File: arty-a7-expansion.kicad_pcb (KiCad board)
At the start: 4 copper layers, 109.2 x 47 mm, 119 parts, among them IC1 TPD8S009DSMR, IC2 PCA9500PW, J1 SJ-43516-SMT-GR, J2 1140084168, J3 SJ-43516-SMT-BE, J4 685119134923, J5 UE27AC54100, U1 TPS61232DRCT, U2 MAX3421EEHJ, U3 CS4344-CZZ, U4 CS5343-CZZ, U5 NC7SZ126P5X, Y1 ABM8G-12.000MHZ-18-D2Y-T

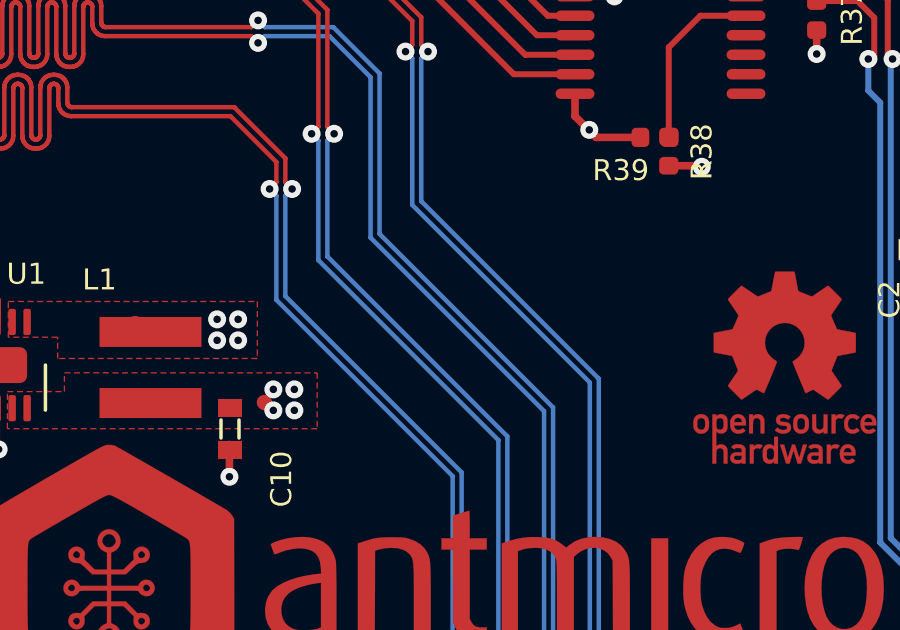
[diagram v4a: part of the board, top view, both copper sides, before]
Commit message: Add PWR indicator
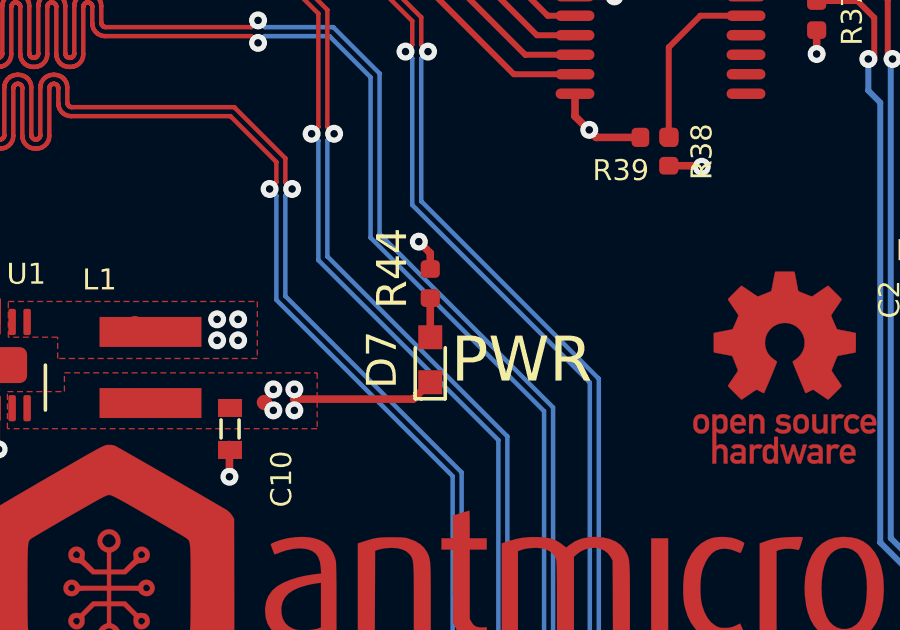
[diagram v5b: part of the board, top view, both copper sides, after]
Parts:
- added D7: LG_L29K-G2J1-24-Z, antmicro-footprints:LED_0603, F.Cu at (158.8, 83.9)
- added R44: R_100R_0402, arty-a7-expansion-footprints:0402-res, F.Cu at (158.8, 81.3)
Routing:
- net +3V3: track 62.6 -> 68.0 mm
- net Net-(D7-Pad2): track 0.00 -> 1.31 mm
- net GND: track 104.3 -> 105.4 mm, vias 49 -> 50
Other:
- board text added: "PWR"
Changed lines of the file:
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@@
-(kicad_pcb (version 20171130) (host pcbnew 5.1.5+dfsg1-2~bpo10+1)
+(kicad_pcb (version 20171130) (host pcbnew 5.1.7-a382d34a8~87~ubuntu18.04.1)
   (general
     (thickness 1.6)
-    (drawings 16)
-    (tracks 3613)
+    (drawings 17)
+    (tracks 3621)
     (zones 0)
-    (modules 119)
-    (nets 122)
+    (modules 121)
+    (nets 123)
   )
   (page A4)
@@
   )
   (layers
-    (0 F.Cu signal)
-    (1 In1.Cu signal)
-    (2 In2.Cu signal)
-    (31 B.Cu signal)
-    (32 B.Adhes user)
-    (33 F.Adhes user)
-    (34 B.Paste user)
-    (35 F.Paste user)
+    (0 F.Cu signal hide)
+    (1 In1.Cu signal hide)
+    (2 In2.Cu signal hide)
+    (31 B.Cu signal hide)
+    (32 B.Adhes user hide)
+    (33 F.Adhes user hide)
+    (34 B.Paste user hide)
+    (35 F.Paste user hide)
     (36 B.SilkS user)
     (37 F.SilkS user)
-    (38 B.Mask user)
-    (39 F.Mask user)
-    (40 Dwgs.User user)
+    (38 B.Mask user hide)
+    (39 F.Mask user hide)
+    (40 Dwgs.User user hide)
     (41 Cmts.User user)
     (42 Eco1.User user)
@@
     (47 F.CrtYd user)
     (48 B.Fab user)
-    (49 F.Fab user)
+    (49 F.Fab user hide)
   )
   (setup
@@
   (net 120 "Net-(IC2-Pad9)")
   (net 121 "Net-(L1-Pad2)")
+  (net 122 "Net-(D7-Pad2)")
   (net_class Default "This is the default net class."
     (clearance 0.15)
@@
     (add_net "Net-(D6-Pad1)")
     (add_net "Net-(D6-Pad2)")
+    (add_net "Net-(D7-Pad2)")
     (add_net "Net-(IC1-Pad14)")
     (add_net "Net-(IC2-Pad10)")
@@
     (add_net "Net-(U2-Pad9)")
   )
+  (module arty-a7-expansion-footprints:0402-res (layer F.Cu)
+    (at 158.81124 81.345693 90)
+    (descr "Resistor SMD 0402 (1005 Metric), square (rectangular) end terminal, IPC_7351 nominal, (Body size source: http://www.tortai-tech.com/upload/download/2011102023233369053.pdf), generated with kicad-footprint-generator")
+    (tags resistor)
+    (attr smd)
+    (fp_text reference R44 (at 0.508 -1.27 90) (layer F.SilkS)
+      (effects (font (size 1 1) (thickness 0.15)))
+    )
+    (fp_text value R_100R_0402 (at 0 1.17 90) (layer F.Fab)
+      (effects (font (size 1 1) (thickness 0.15)))
+    )
+    (fp_line (start 0.93 0.47) (end -0.93 0.47) (layer F.CrtYd) (width 0.05))
+    (fp_line (start 0.93 -0.47) (end 0.93 0.47) (layer F.CrtYd) (width 0.05))
+    (fp_line (start -0.93 -0.47) (end 0.93 -0.47) (layer F.CrtYd) (width 0.05))
+    (fp_line (start -0.93 0.47) (end -0.93 -0.47) (layer F.CrtYd) (width 0.05))
+    (fp_line (start 0.5 0.25) (end -0.5 0.25) (layer F.Fab) (width 0.1))
+    (fp_line (start 0.5 -0.25) (end 0.5 0.25) (layer F.Fab) (width 0.1))
+    (fp_line (start -0.5 -0.25) (end 0.5 -0.25) (layer F.Fab) (width 0.1))
+    (fp_line (start -0.5 0.25) (end -0.5 -0.25) (layer F.Fab) (width 0.1))
+    (fp_text user %R (at 0 0 90) (layer F.Fab)
+      (effects (font (size 0.25 0.25) (thickness 0.04)))
+    )
+    (pad 2 smd roundrect (at 0.485 0 90) (size 0.59 0.64) (layers F.Cu F.Paste F.Mask) (roundrect_rratio 0.25)
+      (net 2 GND))
+    (pad 1 smd roundrect (at -0.485 0 90) (size 0.59 0.64) (layers F.Cu F.Paste F.Mask) (roundrect_rratio 0.25)
+      (net 122 "Net-(D7-Pad2)"))
+    (model ${KIPRJMOD}/lib/3d-models/0402-res.step
+      (offset (xyz 0 0 -0.01))
+      (scale (xyz 1 1 1))
+      (rotate (xyz 0 0 0))
+    )
+  )
+  (module antmicro-footprints:LED_0603 (layer F.Cu)
+    (at 158.81124 83.885693 90)
+    (attr smd)
+    (fp_text reference D7 (at 0 -1.61 90) (layer F.SilkS)
+      (effects (font (size 1 1) (thickness 0.15)))
+    )
+    (fp_text value LG_L29K-G2J1-24-Z (at 0 1.77 90) (layer F.Fab)
+      (effects (font (size 1 1) (thickness 0.15)))
+    )
+    (fp_line (start 0.85 0.4) (end 0.85 -0.4) (layer F.Fab) (width 0.12))
+    (fp_line (start -0.85 0.4) (end -0.85 -0.4) (layer F.Fab) (width 0.12))
+    (fp_line (start -0.85 -0.4) (end 0.85 -0.4) (layer F.Fab) (width 0.12))
+    (fp_line (start -0.85 0.4) (end 0.85 0.4) (layer F.Fab) (width 0.12))
+    (fp_line (start -1.4 0.71) (end -1.4 -0.71) (layer F.CrtYd) (width 0.05))
+    (fp_line (start 1.4 0.71) (end 1.4 -0.71) (layer F.CrtYd) (width 0.05))
+    (fp_line (start -1.4 -0.71) (end 1.4 -0.71) (layer F.CrtYd) (width 0.05))
+    (fp_line (start -1.4 0.71) (end 1.4 0.71) (layer F.CrtYd) (width 0.05))
+    (fp_line (start -1.3 0.5) (end 0.4 0.5) (layer F.SilkS) (width 0.12))
+    (fp_line (start -1.3 -0.3) (end -1.3 0.5) (layer F.SilkS) (width 0.12))
+    (fp_line (start -1.3 -0.5) (end -1.3 -0.3) (layer F.SilkS) (width 0.12))
+    (fp_line (start -1.2 -0.5) (end -1.3 -0.5) (layer F.SilkS) (width 0.12))
+    (fp_line (start -1.1 -0.5) (end -1.2 -0.5) (layer F.SilkS) (width 0.12))
+    (fp_line (start -1.1 -0.5) (end 0.4 -0.5) (layer F.SilkS) (width 0.12))
+    (fp_line (start 0.1 0.2) (end 0.1 0) (layer F.Fab) (width 0.12))
+    (fp_line (start -0.2 0) (end 0.1 0.2) (layer F.Fab) (width 0.12))
+    (fp_line (start 0.1 -0.2) (end -0.2 0) (layer F.Fab) (width 0.12))
+    (fp_line (start 0.1 0) (end 0.1 -0.2) (layer F.Fab) (width 0.12))
+    (fp_line (start 0.5 0) (end 0.1 0) (layer F.Fab) (width 0.12))
+    (fp_line (start -0.3 -0.2) (end -0.3 0.1) (layer F.Fab) (width 0.12))
+    (fp_line (start -0.3 0.2) (end -0.3 0.1) (layer F.Fab) (width 0.12))
+    (pad 2 smd rect (at 0.75 0 90) (size 0.8 0.8) (layers F.Cu F.Paste F.Mask)
+      (net 122 "Net-(D7-Pad2)"))
+    (pad 1 smd rect (at -0.75 0 90) (size 0.8 0.8) (layers F.Cu F.Paste F.Mask)
+      (net 14 +3V3))
+    (model ${ANT3DMDL}/LED0603.step
+      (at (xyz 0 0 0))
+      (scale (xyz 1 1 1))
+      (rotate (xyz 0 0 0))
+    )
+  )
   (module arty-a7-expansion-footprints:XFL4020-102MEB (layer F.Cu)
     (at 149.486241 84.143709 90)
@@
       (effects (font (size 1 1) (thickness 0.15)))
     )
-    (fp_text user %R (at 0 0 90) (layer F.Fab)
-      (effects (font (size 0.25 0.25) (thickness 0.04)))
-    )
     (fp_line (start 0.93 0.47) (end -0.93 0.47) (layer F.CrtYd) (width 0.05))
     (fp_line (start 0.93 -0.47) (end 0.93 0.47) (layer F.CrtYd) (width 0.05))
@@
     (fp_line (start -0.5 -0.25) (end 0.5 -0.25) (layer F.Fab) (width 0.1))
     (fp_line (start -0.5 0.25) (end -0.5 -0.25) (layer F.Fab) (width 0.1))
+    (fp_text user %R (at 0 0 90) (layer F.Fab)
+      (effects (font (size 0.25 0.25) (thickness 0.04)))
+    )
     (pad 2 smd roundrect (at 0.485 0 90) (size 0.59 0.64) (layers F.Cu F.Paste F.Mask) (roundrect_rratio 0.25)
       (net 72 "Net-(C5-Pad1)"))
@@
       (effects (font (size 1 1) (thickness 0.15)))
     )
-    (fp_text user %R (at 0 0) (layer F.Fab)
-      (effects (font (size 0.25 0.25) (thickness 0.04)))
-    )
     (fp_line (start 0.93 0.47) (end -0.93 0.47) (layer F.CrtYd) (width 0.05))
     (fp_line (start 0.93 -0.47) (end 0.93 0.47) (layer F.CrtYd) (width 0.05))
@@
     (fp_line (start -0.5 -0.25) (end 0.5 -0.25) (layer F.Fab) (width 0.1))
     (fp_line (start -0.5 0.25) (end -0.5 -0.25) (layer F.Fab) (width 0.1))
+    (fp_text user %R (at 0 0) (layer F.Fab)
+      (effects (font (size 0.25 0.25) (thickness 0.04)))
+    )
     (pad 2 smd roundrect (at 0.485 0) (size 0.59 0.64) (layers F.Cu F.Paste F.Mask) (roundrect_rratio 0.25)
       (net 70 "Net-(C4-Pad1)"))
@@
       (xy -1.520547 2.559315)) (layer F.Mask) (width 0.01))
   )
+  (gr_text PWR (at 161.85924 83.885693) (layer F.SilkS)
+    (effects (font (size 1.5 1.5) (thickness 0.3)))
+  )
   (gr_line (start 180.501241 73.633709) (end 180.061241 73.633709) (layer F.SilkS) (width 0.15))
   (gr_line (start 180.501241 73.633709) (end 181.271241 73.633709) (layer F.SilkS) (width 0.15))
@@
   (segment (start 185.051241 74.583709) (end 185.221241 74.413709) (width 0.2) (layer F.Cu) (net 2))
   (segment (start 183.961241 74.583709) (end 185.051241 74.583709) (width 0.2) (layer F.Cu) (net 2))
+  (via (at 158.43024 79.948693) (size 0.6) (drill 0.25) (layers F.Cu B.Cu) (net 2))
+  (segment (start 158.81124 80.329693) (end 158.43024 79.948693) (width 0.254) (layer F.Cu) (net 2))
+  (segment (start 158.81124 80.860693) (end 158.81124 80.329693) (width 0.254) (layer F.Cu) (net 2))
   (via (at 153.071241 72.573523) (size 0.6) (drill 0.25) (layers F.Cu B.Cu) (net 3))
   (segment (start 157.121241 74.341575) (end 157.121241 79.691575) (width 0.15) (layer B.Cu) (net 3))
@@
   (segment (start 183.560241 77.004709) (end 183.560241 78.051709) (width 0.2) (layer F.Cu) (net 14))
   (segment (start 183.961241 76.603709) (end 183.560241 77.004709) (width 0.2) (layer F.Cu) (net 14))
+  (segment (start 158.249239 85.197694) (end 158.81124 84.635693) (width 0.254) (layer F.Cu) (net 14))
+  (segment (start 154.281241 85.197694) (end 158.249239 85.197694) (width 0.254) (layer F.Cu) (net 14))
+  (segment (start 154.281241 84.873709) (end 154.281241 85.197694) (width 0.254) (layer F.Cu) (net 14))
+  (segment (start 154.281241 85.197694) (end 154.281241 85.573709) (width 0.254) (layer F.Cu) (net 14))
   (segment (start 123.82374 71.783709) (end 124.17374 71.433709) (width 0.15) (layer F.Cu) (net 15))
   (segment (start 119.383375 71.783709) (end 123.82374 71.783709) (width 0.15) (layer F.Cu) (net 15))
@@
   (via (at 151.706241 83.238709) (size 0.6) (drill 0.25) (layers F.Cu B.Cu) (net 121))
   (via (at 152.406241 83.238709) (size 0.6) (drill 0.25) (layers F.Cu B.Cu) (net 121))
+  (segment (start 158.81124 83.135693) (end 158.81124 81.830693) (width 0.254) (layer F.Cu) (net 122))
   (zone (net 2) (net_name GND) (layer In1.Cu) (hatch edge 0.508)
     (connect_pads (clearance 0.508))
